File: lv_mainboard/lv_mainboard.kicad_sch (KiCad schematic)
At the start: 42 parts, among them J1 DE9_Plug, J13 Conn_02x10_Odd_Even, J14 Conn_02x10_Odd_Even, J15 Conn_02x10_Counter_Clockwise, J2 DE9_Plug, J3 DE9_Plug, J4 DE9_Plug, J5 DE9_Plug, J6 Conn_02x10_Odd_Even, J7 Conn_02x10_Odd_Even

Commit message: add layout
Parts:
- added H1, H2, H3, H4: MountingHole, MountingHole:MountingHole_4.3mm_M4_Pad, symbol Mechanical:MountingHole
- J1, J2, J3, J4, J5: footprint Connector_Dsub:DSUB-9_Female_Vertical_P2.77x2.84mm -> Connector_Dsub:DSUB-9_Female_Horizontal_P2.77x2.84mm_EdgePinOffset7.70mm_Housed_MountingHolesOffset9.12mm
- J13, J14, J6, J7: footprint Connector_PinHeader_2.54mm:PinHeader_2x10_P2.54mm_Vertical -> Connector_PinSocket_2.54mm:PinSocket_2x10_P2.54mm_Vertical
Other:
- moved on the sheet: J14, J6, R1, R2, R3, R4, R5, R6

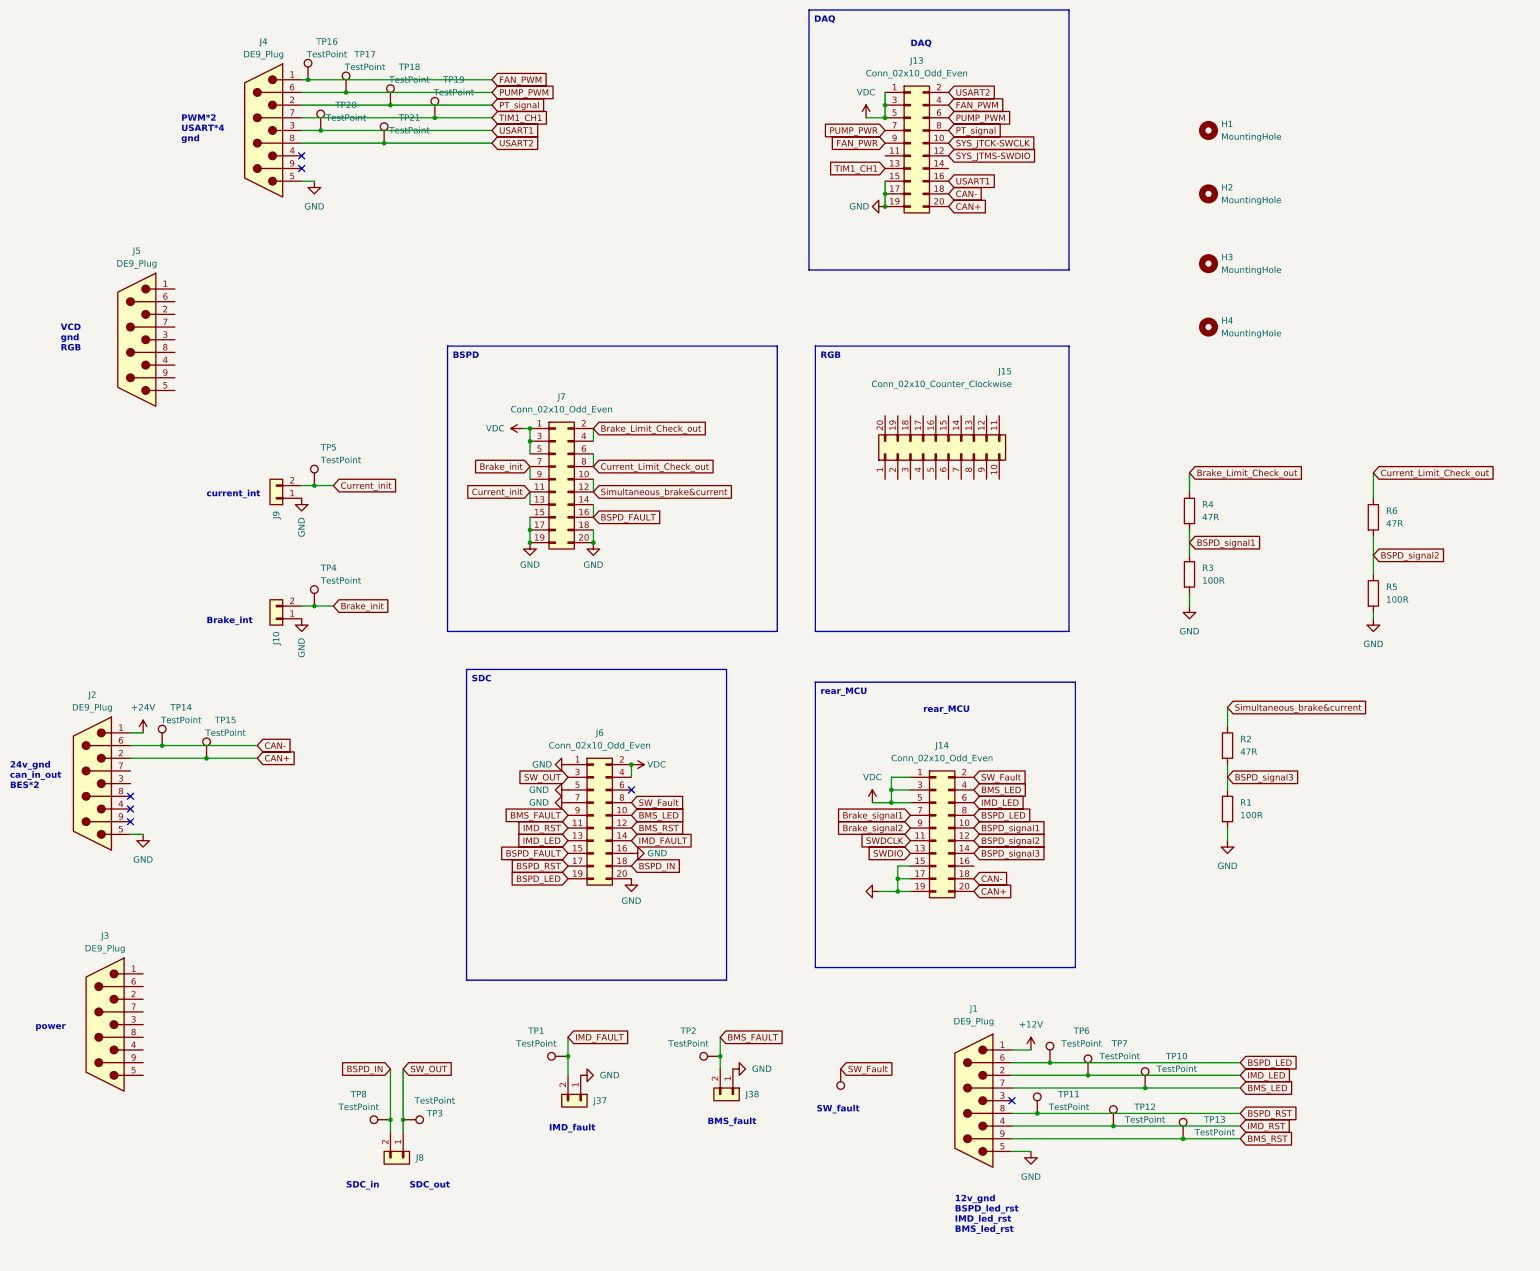
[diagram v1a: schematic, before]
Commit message: add mounting hole
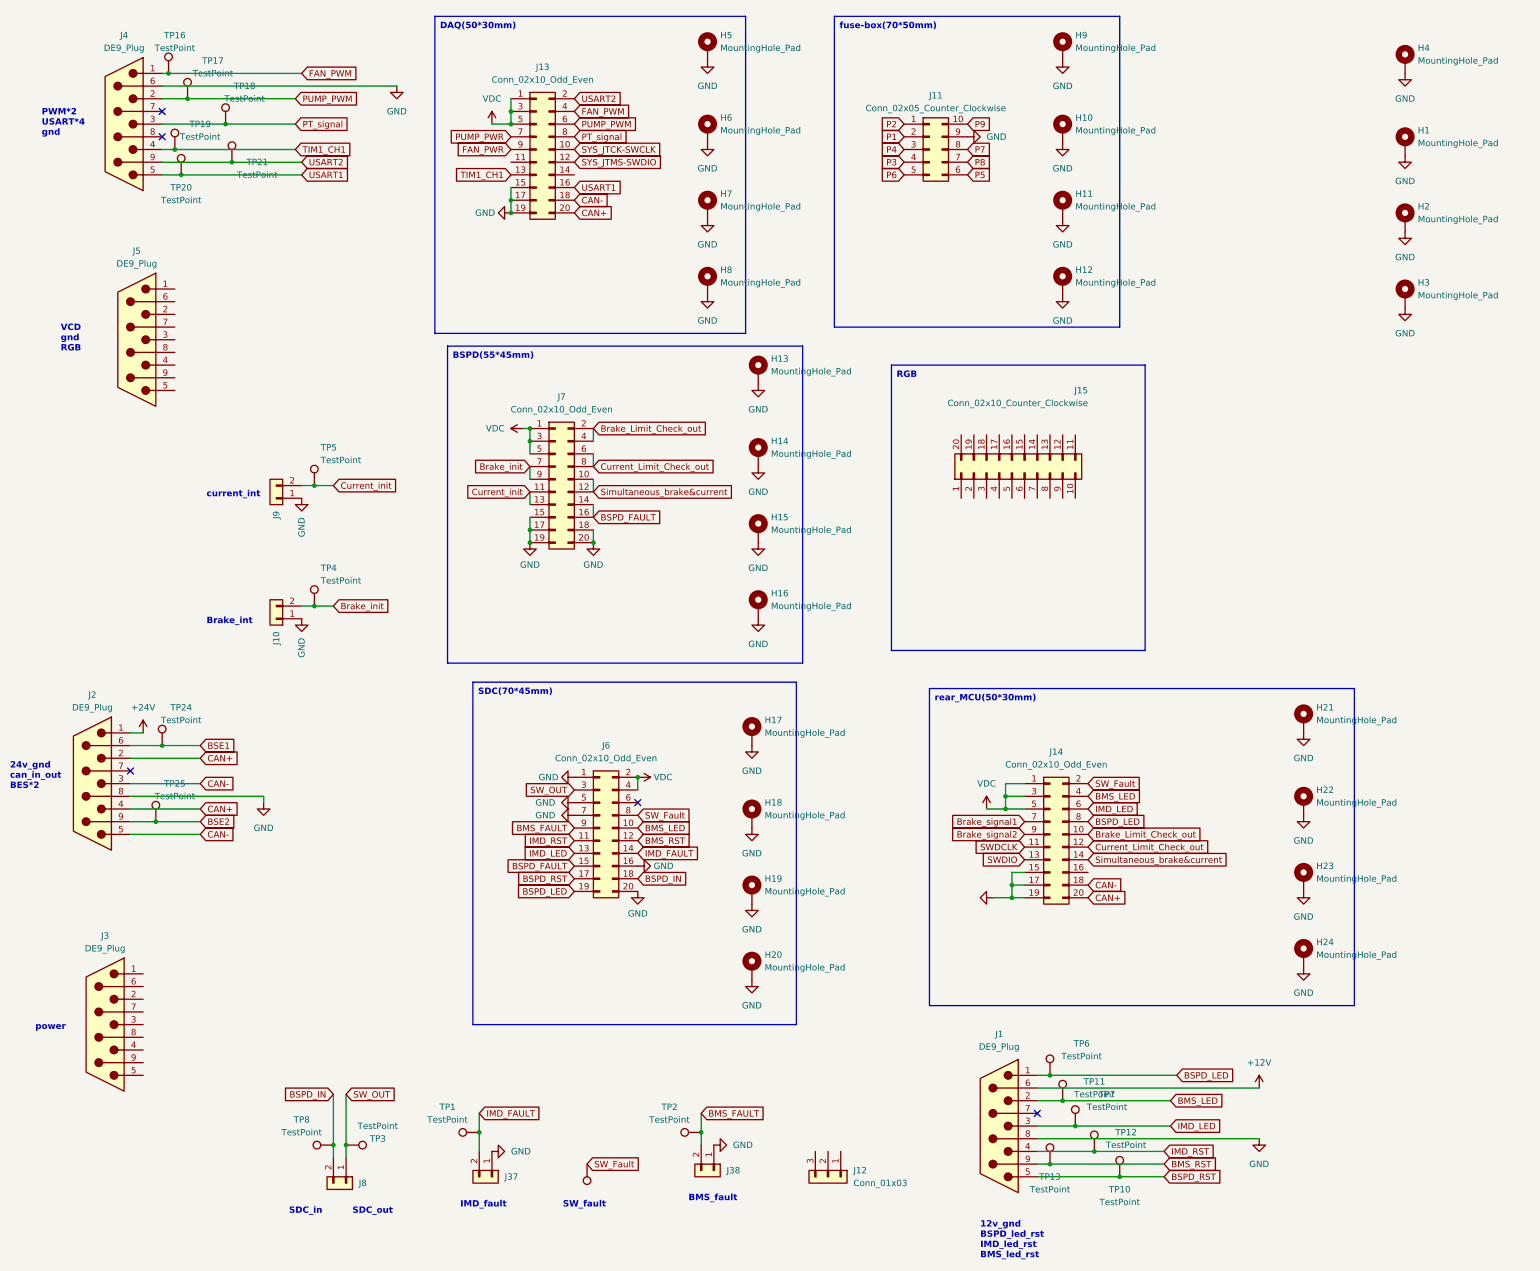
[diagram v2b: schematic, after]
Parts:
- removed H1, H2, H3, H4: MountingHole, MountingHole:MountingHole_4.3mm_M4_Pad, symbol Mechanical:MountingHole
- removed R1, R3, R5: 100R, Resistor_SMD:R_0603_1608Metric, symbol Device:R
- removed R2, R4, R6: 47R, Resistor_SMD:R_0603_1608Metric, symbol Device:R
- removed TP14, TP15: TestPoint, TestPoint:TestPoint_Keystone_5000-5004_Miniature, symbol Connector:TestPoint
- added H1, H2, H3, H4: MountingHole_Pad, MountingHole:MountingHole_4.3mm_M4_Pad, symbol Mechanical:MountingHole_Pad
- added H10, H11, H12, H13, H14, H15, H16, H17, H18, H19, H20, H21, H22, H23, H24, H5, H6, H7, H8, H9: MountingHole_Pad, MountingHole:MountingHole_3.2mm_M3_Pad, symbol Mechanical:MountingHole_Pad
- added J11: Conn_02x05_Counter_Clockwise, Connector_PinSocket_2.54mm:PinSocket_2x05_P2.54mm_Vertical, symbol Connector_Generic:Conn_02x05_Counter_Clockwise
- added J12: Conn_01x03, Connector_JST:JST_EH_B3B-EH-A_1x03_P2.50mm_Vertical, symbol Connector_Generic:Conn_01x03
- added TP24, TP25: TestPoint, TestPoint:TestPoint_Keystone_5000-5004_Miniature, symbol Connector:TestPoint
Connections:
- net BSPD_signal1 is gone; now on net Brake_Limit_Check_out: J14.10 (Pin_10)
- net BSPD_signal2 is gone; now on net Current_Limit_Check_out: J14.12 (Pin_12)
- net BSPD_signal3 is gone; now on net Simultaneous_brake&current: J14.14 (Pin_14)
- net +12V: now also J1.6; no longer J1.1
- net BMS_LED: now also J1.2, TP11.1; no longer J1.7, TP10.1
- net BSPD_LED: now also J1.1; no longer J1.6
- net BSPD_RST: now also J1.5, TP10.1; no longer J1.8, TP11.1
- net CAN+: now also J2.4
- net CAN-: now also J2.3, J2.5; no longer J2.6
- net GND: now also J1.8, J2.8, J4.6, H1.1, H10.1, H11.1, H12.1, H13.1, H14.1, H15.1, H16.1, H17.1, H18.1, H19.1, H2.1, H20.1, H21.1, H22.1, H23.1, H24.1, H3.1, H4.1, H5.1, H6.1, H7.1, H8.1, H9.1, J11.9 (Pin_9); no longer J1.5, J2.5, J4.5
- net IMD_LED: now also J1.3; no longer J1.2
- net PT_signal: now also J4.3; no longer J4.2
- net PUMP_PWM: now also J4.2; no longer J4.6
- net TIM1_CH1: now also J4.4; no longer J4.7
- net USART1: now also J4.5; no longer J4.3
- net USART2: now also J4.9; no longer J4.8
- net BSE2: now reaches J2.9
- net BSE2: now also TP25.1
- new net BSE1: J2.6, TP24.1
- new net P1: J11.2 (Pin_2)
- new net P2: J11.1 (Pin_1)
- new net P3: J11.4 (Pin_4)
- new net P4: J11.3 (Pin_3)
- new net P5: J11.6 (Pin_6)
- new net P6: J11.5 (Pin_5)
- new net P7: J11.8 (Pin_8)
- new net P8: J11.7 (Pin_7)
- new net P9: J11.10 (Pin_10)
- no-connect marks 7 -> 5
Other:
- note removed: "DAQ"
- note removed: "rear_MCU"
- moved on the sheet: J1, J13, J14, J15, J37, J38, J4, J6, J8, TP1, TP10, TP11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

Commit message: v2025.5 finish schemetic
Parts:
- removed J1, J2, J3, J4, J5: DE9_Plug, Connector_Dsub:DSUB-9_Female_Horizontal_P2.77x2.84mm_EdgePinOffset7.70mm_Housed_MountingHolesOffset9.12mm, symbol Connector:DE9_Plug
- removed J12: Conn_01x03, Connector_JST:JST_EH_B3B-EH-A_1x03_P2.50mm_Vertical, symbol Connector_Generic:Conn_01x03
- removed J14: Conn_02x10_Odd_Even, Connector_PinSocket_2.54mm:PinSocket_2x10_P2.54mm_Vertical, symbol Connector_Generic:Conn_02x10_Odd_Even
- removed J15: Conn_02x10_Counter_Clockwise, Connector_PinSocket_2.54mm:PinSocket_2x10_P2.54mm_Vertical, symbol Connector_Generic:Conn_02x10_Counter_Clockwise
- removed J37, J38, J8, J9: ~, Connector_JST:JST_EH_B2B-EH-A_1x02_P2.50mm_Vertical, symbol Connector_Generic:Conn_01x02
- removed TP1, TP10, TP11, TP12, TP13, TP16, TP17, TP18, TP19, TP2, TP20, TP21, TP24, TP25, TP3, TP4, TP5, TP6, TP7, TP8, TP9: TestPoint, TestPoint:TestPoint_Keystone_5000-5004_Miniature, symbol Connector:TestPoint
- added J1: Conn_01x02, Connector_JST:JST_XH_B2B-XH-A_1x02_P2.50mm_Vertical, symbol Connector_Generic:Conn_01x02
- added J12, J14, J15, J16, J4, J8: Conn_01x04, Connector_JST:JST_XH_B4B-XH-A_1x04_P2.50mm_Vertical, symbol Connector_Generic:Conn_01x04
- added J2: Conn_02x10_Odd_Even, Connector_PinSocket_2.54mm:PinSocket_2x10_P2.54mm_Vertical, symbol Connector_Generic:Conn_02x10_Odd_Even
- added J3: Conn_01x03, Connector_JST:JST_XH_B3B-XH-A_1x03_P2.50mm_Vertical, symbol Connector_Generic:Conn_01x03
- added J5: Conn_01x05, Connector_JST:JST_XH_B5B-XH-A_1x05_P2.50mm_Vertical, symbol Connector_Generic:Conn_01x05
- added J9: DE9_Plug_MountingHoles, Connector_Dsub:DSUB-9_Female_Horizontal_P2.77x2.84mm_EdgePinOffset7.70mm_Housed_MountingHolesOffset9.12mm, symbol Connector:DE9_Plug_MountingHoles
- added R1, R2: R, Resistor_SMD:R_0603_1608Metric, symbol Device:R
- H1, H2, H3, H4: footprint MountingHole:MountingHole_4.3mm_M4_Pad -> MountingHole:MountingHole_4.3mm_M4_ISO7380_Pad
- H10, H11, H12, H13, H14, H15, H16, H17, H18, H19, H20, H21, H22, H23, H24, H5, H6, H7, H8, H9: footprint MountingHole:MountingHole_3.2mm_M3_Pad -> MountingHole:MountingHole_3.2mm_M3_ISO7380_Pad
- J10: value ~ -> PWR; footprint Connector_JST:JST_EH_B2B-EH-A_1x02_P2.50mm_Vertical -> Connector_AMASS:AMASS_XT60-M_1x02_P7.20mm_Vertical
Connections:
- net BSPD_IN is gone; now on net BSPD_RST: J6.18 (Pin_18)
- net SW_OUT is gone; now on net P3_SDCPCB: J6.3 (Pin_3)
- net +24V: now also J8.4 (Pin_4)
- net BMS_FAULT: now also J6.10 (Pin_10), J4.4 (Pin_4); no longer J6.9 (Pin_9)
- net BMS_LED: now also J6.9 (Pin_9), J14.2 (Pin_2); no longer J6.10 (Pin_10)
- net BMS_RST: now also J6.11 (Pin_11), J14.3 (Pin_3); no longer J6.12 (Pin_12)
- net BSPD_FAULT: now also J6.16 (Pin_16); no longer J6.15 (Pin_15), J7.14 (Pin_14), J7.16 (Pin_16)
- net BSPD_LED: now also J6.20 (Pin_20), J12.2 (Pin_2); no longer J6.19 (Pin_19)
- net BSPD_RST: now also J12.3 (Pin_3); no longer J6.17 (Pin_17)
- net CAN+: now also J2.20 (Pin_20), J9.7
- net CAN-: now also J2.18 (Pin_18), J9.2
- net FAN_PWR: now also J3.2 (Pin_2)
- net GND: now also J10.2 (Pin_2), J6.15 (Pin_15), J6.19 (Pin_19), J6.2 (Pin_2), J6.6 (Pin_6), J6.8 (Pin_8), J1.1 (Pin_1), J12.1 (Pin_1), J14.1 (Pin_1), J15.1 (Pin_1), J16.1 (Pin_1), J2.15 (Pin_15), J2.17 (Pin_17), J2.19 (Pin_19), J3.1 (Pin_1), J4.1 (Pin_1), J5.1 (Pin_1), J8.1 (Pin_1), J9.3, J9.5, J9.6, R1.1, R2.1; no longer J10.1 (Pin_1), J6.1 (Pin_1), J6.16 (Pin_16), J6.20 (Pin_20), J6.5 (Pin_5), J6.7 (Pin_7), J7.15 (Pin_15), J7.17 (Pin_17), J7.18 (Pin_18), J7.19 (Pin_19), J7.20 (Pin_20)
- net IMD_FAULT: now also J6.13 (Pin_13), J4.3 (Pin_3); no longer J6.14 (Pin_14)
- net IMD_LED: now also J6.14 (Pin_14), J16.2 (Pin_2); no longer J6.13 (Pin_13)
- net IMD_RST: now also J6.12 (Pin_12), J16.3 (Pin_3); no longer J6.11 (Pin_11)
- net P7: now also J15.4 (Pin_4)
- net P8: now also J15.3 (Pin_3)
- net P9: now also J15.2 (Pin_2)
- net PT_signal: now also J5.4 (Pin_4)
- net PUMP_PWR: now also J3.3 (Pin_3)
- net SWDCLK: now also J2.11 (Pin_11)
- net SWDIO: now also J2.13 (Pin_13)
- net SW_Fault: now also J6.7 (Pin_7); no longer J6.8 (Pin_8)
- net TIM1_CH1: now also J5.3 (Pin_3)
- net USART1: now also J5.2 (Pin_2)
- net USART2: now also J5.5 (Pin_5)
- net Brake_Limit_Check_out renamed BSE_L_init
- net BSE_L_init: now also J9.1, R1.2; no longer J7.4 (Pin_4)
- removed net Brake_init: J10.2 (Pin_2), J7.7 (Pin_7), J7.9 (Pin_9)
- net Current_Limit_Check_out: no longer names the net of J7.8 (Pin_8)
- net Current_Limit_Check_out: no longer J7.6 (Pin_6)
- net Current_init: no longer names the net of J7.11 (Pin_11)
- net Current_init: no longer J7.13 (Pin_13)
- net P1 renamed P1_DAQ
- net P1_DAQ: now also J13.1 (Pin_1), J13.3 (Pin_3), J13.5 (Pin_5)
- net P2 renamed P2_BSPD
- net P2_BSPD: now also J7.1 (Pin_1), J7.3 (Pin_3)
- net P3 renamed P3_SDCPCB
- net P3_SDCPCB: now also J6.1 (Pin_1)
- net P4 renamed P4_SDCOUT
- net P4_SDCOUT: now also J6.17 (Pin_17)
- net P5 renamed P5_MCU
- net P5_MCU: now also J2.1 (Pin_1), J2.3 (Pin_3), J2.5 (Pin_5)
- net P6 renamed P6_sideboard
- net P6_sideboard: now also J12.4 (Pin_4), J14.4 (Pin_4), J16.4 (Pin_4)
- net Simultaneous_brake&current: no longer names the net of J7.12 (Pin_12)
- net Simultaneous_brake&current: no longer J7.10 (Pin_10)
- removed net VDC: J13.1 (Pin_1), J13.3 (Pin_3), J13.5 (Pin_5), J6.2 (Pin_2), J6.4 (Pin_4), J7.1 (Pin_1), J7.3 (Pin_3), J7.5 (Pin_5)
- new net +3.3V: J9.9
- new net BMS_Fault: J2.4 (Pin_4)
- new net BSE_L_Fault: J2.10 (Pin_10), J7.6 (Pin_6)
- new net BSE_R_Fault: J2.12 (Pin_12), J7.10 (Pin_10)
- new net BSE_R_init: J7.4 (Pin_4), J9.8, R2.2
- new net BSPD: J2.8 (Pin_8), J7.18 (Pin_18), J7.20 (Pin_20)
- new net BSPD_signal3: J2.14 (Pin_14), J7.14 (Pin_14)
- new net BSPD_signal4: J2.7 (Pin_7), J7.16 (Pin_16)
- new net IMD_Fault: J2.6 (Pin_6)
- new net SDC_OUT: J10.1 (Pin_1), J6.4 (Pin_4)
- new net SW_signal: J2.2 (Pin_2)
- new net TSAL: J8.2 (Pin_2)
- new net TSSI: J2.16 (Pin_16), J4.2 (Pin_2), J8.3 (Pin_3)
- new net current_init: J1.2 (Pin_2), J7.19 (Pin_19)
- no-connect marks 5 -> 4
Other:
- note added: "15V out"
- note added: "DAQ"
- note added: "PWM"
- note added: "SDC out"
- note added: "To mainhoop light"
- note added: "from ACC box"
- note added: "from HV box"
- note added: "sideboard"
- note removed: "12v_gnd BSPD_led_rst IMD_led_rst BMS_led_rst"
- note removed: "24v_gnd can_in_out BES*2"
- note removed: "BMS_fault"
- note removed: "Brake_int"
- note removed: "IMD_fault"
- note removed: "PWM*2 USART*4 gnd"
- note removed: "SDC_in"
- note removed: "SDC_out"
- note removed: "SW_fault"
- note removed: "VCD gnd RGB"
- note removed: "current_int"
- note removed: "power"
- moved on the sheet: H1, H10, H11, H12, H13, H14, H15, H16, H17, H18, H19, H2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

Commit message: finish layout
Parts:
- added C1, C3: 1u, Resistor_SMD:R_0603_1608Metric, symbol Device:C
- added C2, C4: 10u, Resistor_SMD:R_0805_2012Metric, symbol Device:C
- added C5: 1u, Capacitor_SMD:C_0603_1608Metric_Pad1.08x0.95mm_HandSolder, symbol Device:C_Small
- added C6: 10u, Capacitor_SMD:C_0805_2012Metric_Pad1.18x1.45mm_HandSolder, symbol Device:C_Small
- added J17: Conn_01x04, Connector_JST:JST_XH_B4B-XH-A_1x04_P2.50mm_Vertical, symbol Connector_Generic:Conn_01x04
- added R3, R5: 100k, Resistor_SMD:R_0603_1608Metric, symbol Device:R
- added R4: 301k, Resistor_SMD:R_0603_1608Metric, symbol Device:R
- added R6: 165k, Resistor_SMD:R_0603_1608Metric, symbol Device:R
- added R7: 100k, Resistor_SMD:R_0603_1608Metric, symbol Device:R_Small
- added R8: 866k, Resistor_SMD:R_0603_1608Metric, symbol Device:R_Small
- added TP1, TP2, TP3: TestPoint, TestPoint:TestPoint_THTPad_D1.5mm_Drill0.7mm, symbol Connector:TestPoint
- added U1, U2, U3: AP2204K-ADJ, Package_TO_SOT_SMD:SOT-23-5, symbol Regulator_Linear:AP2204K-ADJ
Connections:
- net BMS_Fault is gone; now on net BMS_FAULT: J2.4 (Pin_4)
- net BSPD_FAULT is gone; now on net BSPD: J6.16 (Pin_16)
- net IMD_Fault is gone; now on net IMD_FAULT: J2.6 (Pin_6)
- net BMS_FAULT: now also J4.3 (Pin_3); no longer J4.4 (Pin_4)
- net GND: now also C1.2, C2.2, C3.2, C4.2, C5.2, C6.2, J17.1 (Pin_1), R3.1, R5.1, R7.1, U1.2 (GND), U2.2 (GND), U3.2 (GND)
- net IMD_FAULT: now also J4.4 (Pin_4); no longer J4.3 (Pin_3)
- net P3_SDCPCB: now also J6.17 (Pin_17)
- net P5_MCU: now also C1.1, C5.1, U1.1 (VIN), U1.3 (EN), U3.1 (VIN), U3.3 (EN)
- net P7: now also J15.2 (Pin_2); no longer J15.4 (Pin_4)
- net P8: now also J15.4 (Pin_4); no longer J15.3 (Pin_3)
- net P9: now also J15.3 (Pin_3); no longer J15.2 (Pin_2)
- net TSAL: now also J4.2 (Pin_2)
- net TSSI: no longer J4.2 (Pin_2)
- net +3.3V renamed +3V3
- net +3V3: now also C4.1, J17.2 (Pin_2), R6.1, TP3.1, U2.5 (VOUT)
- net P4_SDCOUT renamed P4_RGB
- net P4_RGB: no longer J6.17 (Pin_17)
- new net: R5.2, R6.2, U2.4 (ADJ)
- new net: R7.2, R8.2, U3.4 (ADJ)
- new net: R3.2, R4.2, U1.4 (ADJ)
- new net +12V: C6.1, J17.4 (Pin_4), R8.1, TP2.1, U3.5 (VOUT)
- new net +5V: C2.1, C3.1, J17.3 (Pin_3), R4.1, TP1.1, U1.5 (VOUT), U2.1 (VIN), U2.3 (EN)
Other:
- moved on the sheet: H21, H22, H23, H24

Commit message: v2025.6, add vdd to accbox
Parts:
- removed J15: Conn_01x04, Connector_JST:JST_XH_B4B-XH-A_1x04_P2.50mm_Vertical, symbol Connector_Generic:Conn_01x04
- added J15, J19: PWR, Connector_AMASS:AMASS_XT60-M_1x02_P7.20mm_Vertical, symbol Connector_Generic:Conn_01x02
- added J18: Conn_01x02, Connector_JST:JST_XH_B2B-XH-A_1x02_P2.50mm_Vertical, symbol Connector_Generic:Conn_01x02
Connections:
- net GND: now also J15.2 (Pin_2), J18.1 (Pin_1), J19.2 (Pin_2)
- net P8: now also J15.1 (Pin_1)
- net P9: now also J19.1 (Pin_1)
- net P7 renamed P7_ACC
- net P7_ACC: now also J18.2 (Pin_2)
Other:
- note removed: "15V out"
